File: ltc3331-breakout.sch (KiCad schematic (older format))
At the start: 61 parts, among them IC1 LTC3331, J1 CONN_01X04, J10 CONN_01X02_FEMALE, J11 CONN_01X04, J12 CONN_01X03, J13 CONN_01X03, J14 CONN_01X03, J15 CONN_02X12, J16 CONN_02X08, J17 CONN_02X08, J18 CONN_02X08, J19 CONN_02X08, J2 CONN_01X03, J20 CONN_02X04, J3 CONN_01X03, J4 CONN_01X03, J5 CONN_01X02, J6 CONN_01X04, J7 CONN_01X03, J8 CONN_01X03, J9 CONN_01X03, U1 NC7SZ58, U2 NC7SZ58

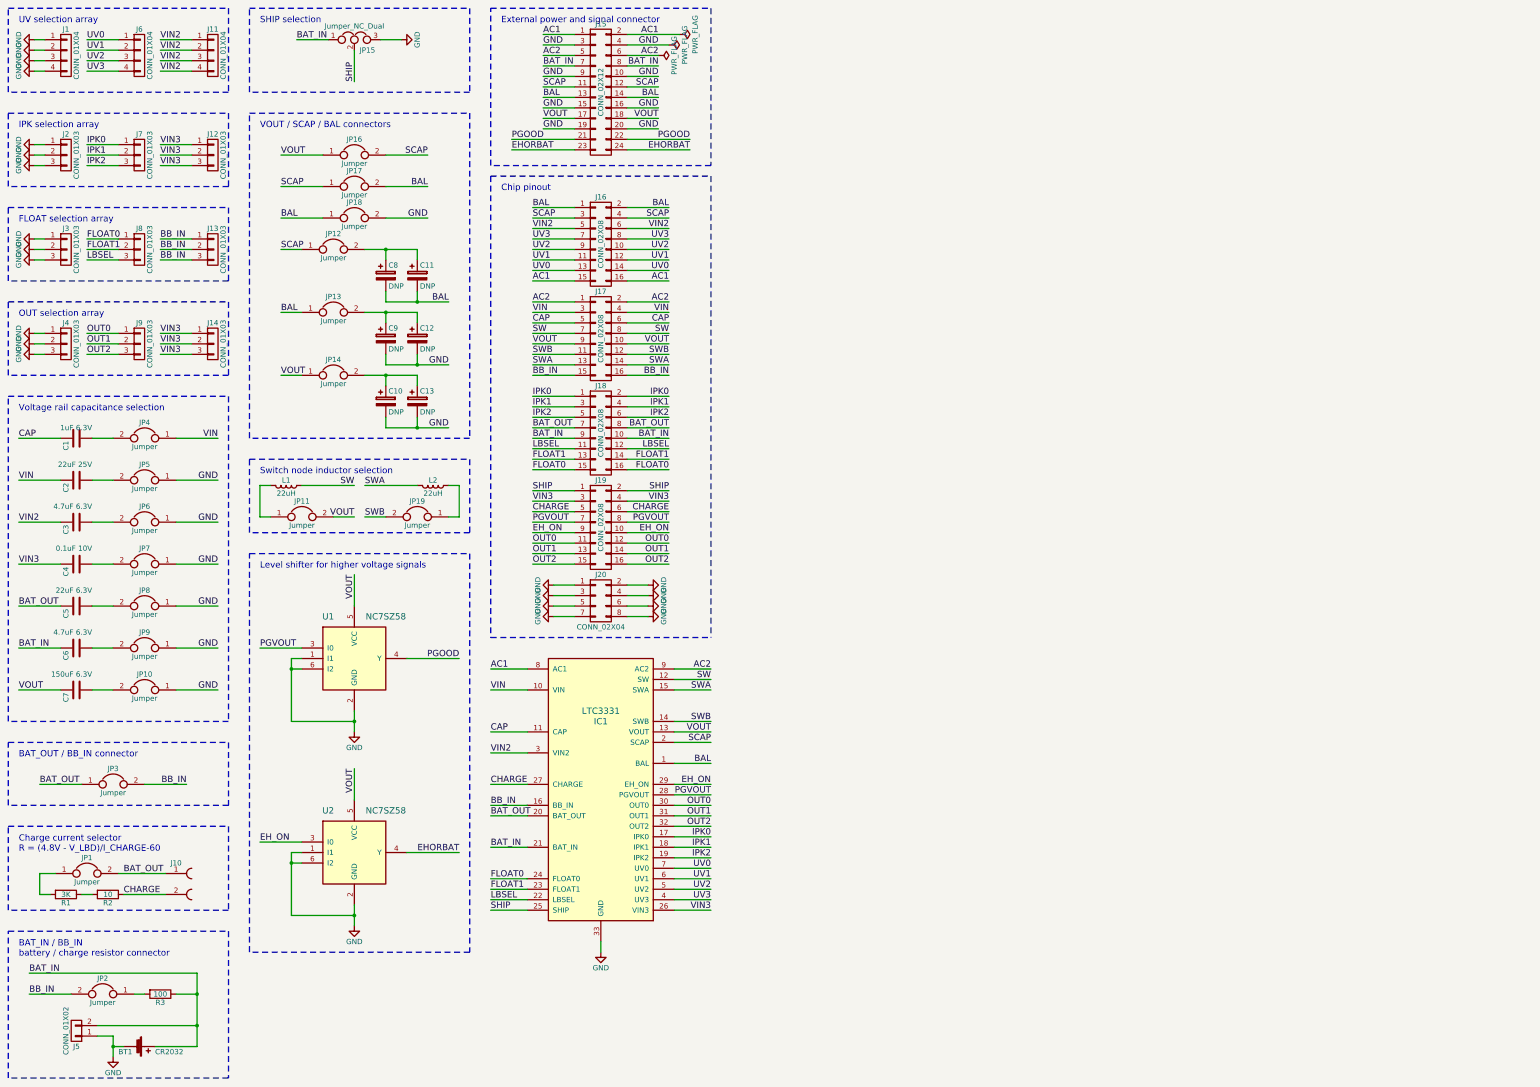
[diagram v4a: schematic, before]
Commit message: schematic: applied some errata from v0.1
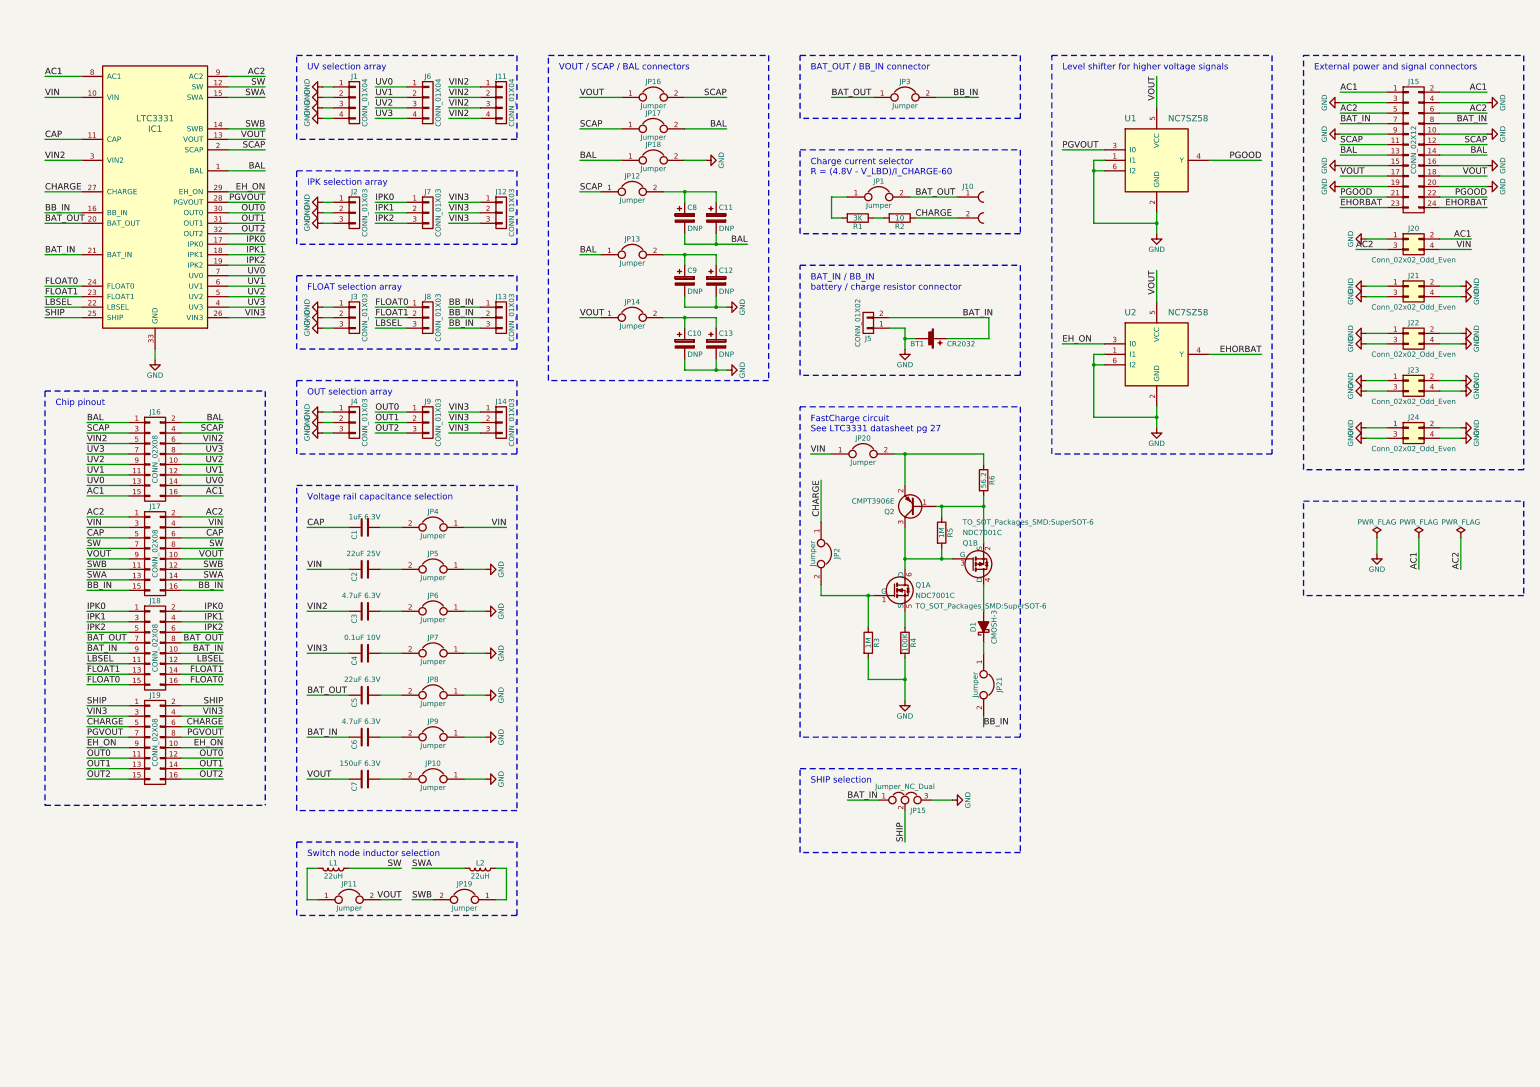
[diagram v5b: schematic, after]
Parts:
- removed J20: CONN_02X04, Pin_Headers:Pin_Header_Straight_2x04_Pitch2.54mm, symbol CONN_02X04
- added D1: CMOSH-3, Diodes_SMD:D_SOD-523, symbol D_Schottky_ALT
- added J20, J21, J22, J23, J24: Conn_02x02_Odd_Even, Pin_Headers:Pin_Header_Straight_2x02_Pitch2.54mm, symbol Conn_02x02_Odd_Even
- added JP20, JP21: Jumper, Pin_Headers:Pin_Header_Straight_1x02_Pitch2.54mm, symbol Jumper
- added Q1: NDC7001C, TO_SOT_Packages_SMD:SuperSOT-6, symbol NDC7001C
- added Q2: CMPT3906E, TO_SOT_Packages_SMD:SOT-23, symbol Q_PNP_BEC
- added R4: 100K, Resistors_SMD:R_1206_HandSoldering, symbol R
- added R5: 1M, Resistors_SMD:R_1206_HandSoldering, symbol R
- added R6: 56.2, Resistors_SMD:R_1206_HandSoldering, symbol R
- R3: value 100 -> 1M
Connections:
- net AC1: now also J20.2 (Pin_2)
- net AC2: now also J20.3 (Pin_3)
- net BAT_IN: no longer R3.1
- net BB_IN: now also JP21.2; no longer JP2.2
- net CHARGE: now also JP2.1
- net GND: now also R3.2, J20.1 (Pin_1), J21.1 (Pin_1), J21.2 (Pin_2), J21.3 (Pin_3), J21.4 (Pin_4), J22.1 (Pin_1), J22.2 (Pin_2), J22.3 (Pin_3), J22.4 (Pin_4), J23.1 (Pin_1), J23.2 (Pin_2), J23.3 (Pin_3), J23.4 (Pin_4), J24.1 (Pin_1), J24.2 (Pin_2), J24.3 (Pin_3), J24.4 (Pin_4), R4.2
- net VIN: now also J20.4 (Pin_4), JP20.1
- new net: D1.1 (K), JP21.1
- new net: D1.2 (A), Q1.4 (D)
- new net: JP2.2, Q1.1 (G), R3.1
- new net: Q1.5 (S), R4.1
- new net: Q1.3 (G), Q1.6 (D), Q2.3 (C), R5.2
- new net: Q1.2 (S), Q2.1 (B), R5.1, R6.2
- new net: JP20.2, Q2.2 (E), R6.1
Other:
- note added: "External power and signal connectors"
- note added: "FastCharge circuit\nSee LTC3331 datasheet pg 27"
- note removed: "External power and signal connector"
- moved on the sheet: BT1, C1, C10, C11, C12, C13, C2, C3, C4, C5, C6, C7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

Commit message: routed changes
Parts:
- renumbered J16 to J1, J7 to J10, J8 to J11, J9 to J12, J11 to J13, J12 to J14, J13 to J15, J14 to J16, J5 to J17, J10 to J18, J20 to J19, J17 to J2, J21 to J20, J22 to J21, J23 to J22, J24 to J23, J15 to J24, J18 to J3, J19 to J4, J1 to J5, J2 to J6, J3 to J7, J4 to J8, J6 to J9, JP11 to JP1, JP12 to JP10, JP13 to JP11, JP14 to JP12, JP16 to JP13, JP17 to JP14, JP18 to JP15, JP2 to JP16, JP20 to JP17, JP1 to JP18, JP3 to JP19, JP4 to JP2, JP15 to JP20, JP5 to JP3, JP6 to JP4, JP7 to JP5, JP8 to JP6, JP9 to JP7, JP10 to JP8, JP19 to JP9, R3 to R2, R2 to R3

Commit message: replaced some capacitors with generic footprint, rerouted
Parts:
- C2, C3, C5, C6, C7: footprint Capacitors_SMD:C_1206_HandSoldering -> footprints:CAP_Generic_SMD_Radial_D10.0mm_P2.50mm_P5.00mm
